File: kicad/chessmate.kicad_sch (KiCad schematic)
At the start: 41 parts, among them J1 7SegBtm, J2 Power Jack, J3 7SegTop, Q1 2N2222, Q2 2N2222, Q3 2N2222, Q4 2N2222, Q5 2N2222, SW1 F6, SW10 ENTER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

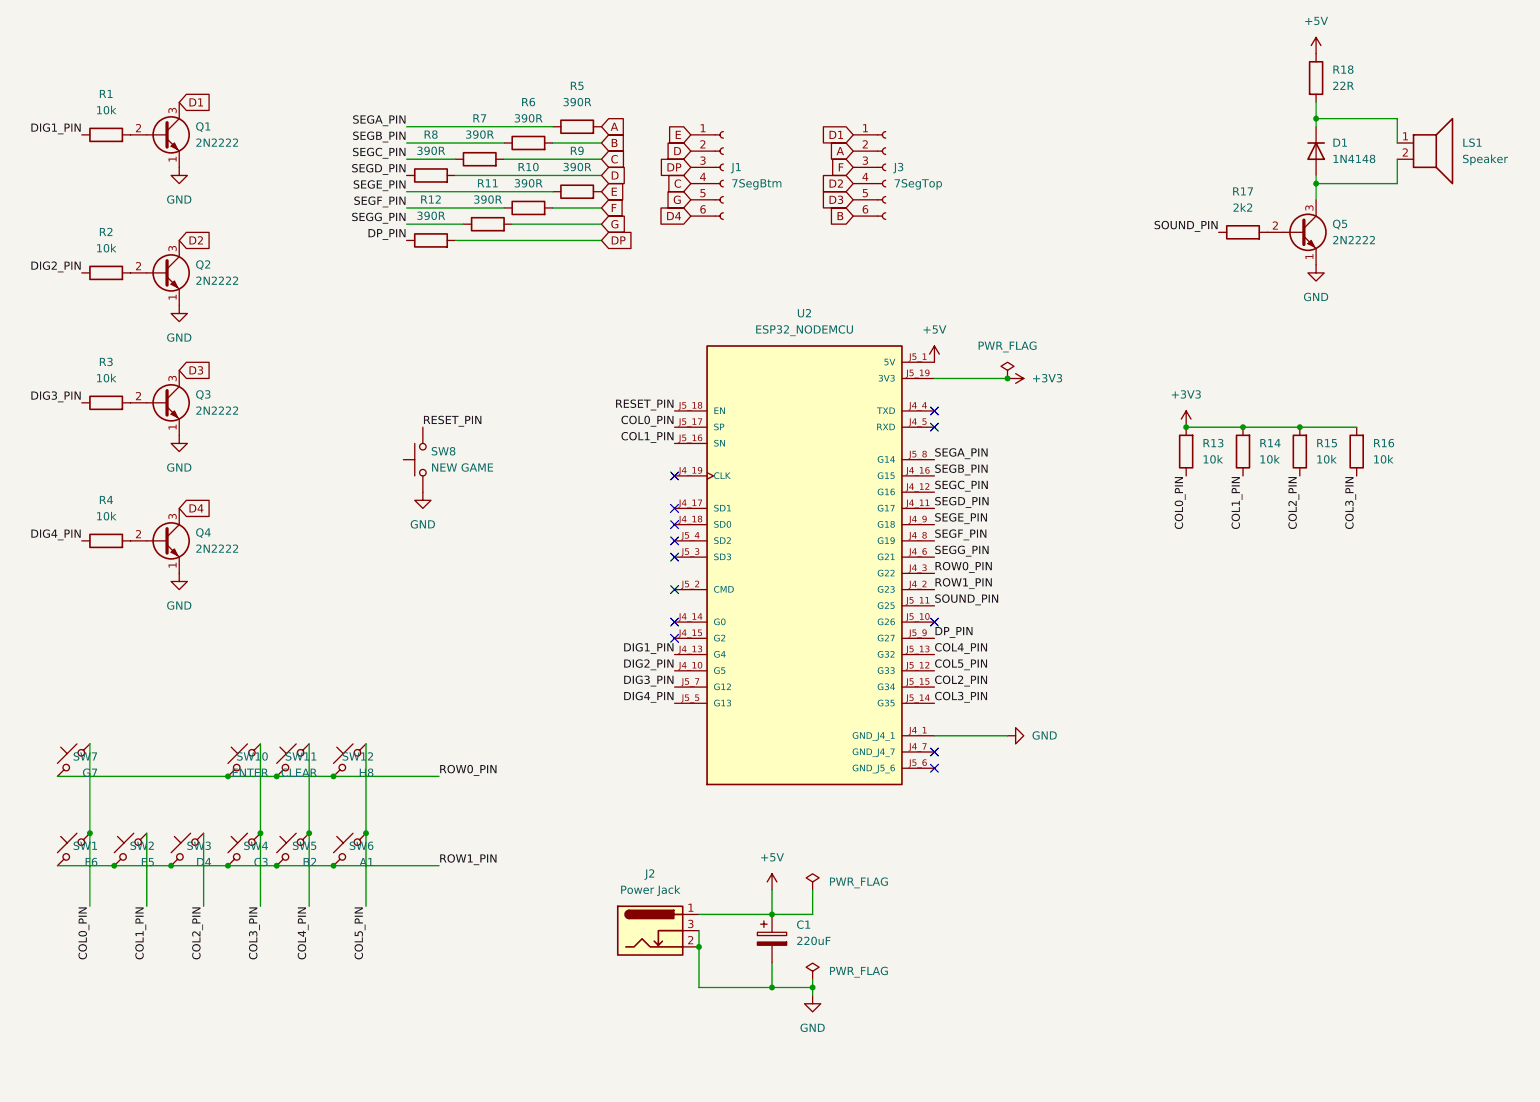
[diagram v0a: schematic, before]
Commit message: update nodemcu footprint
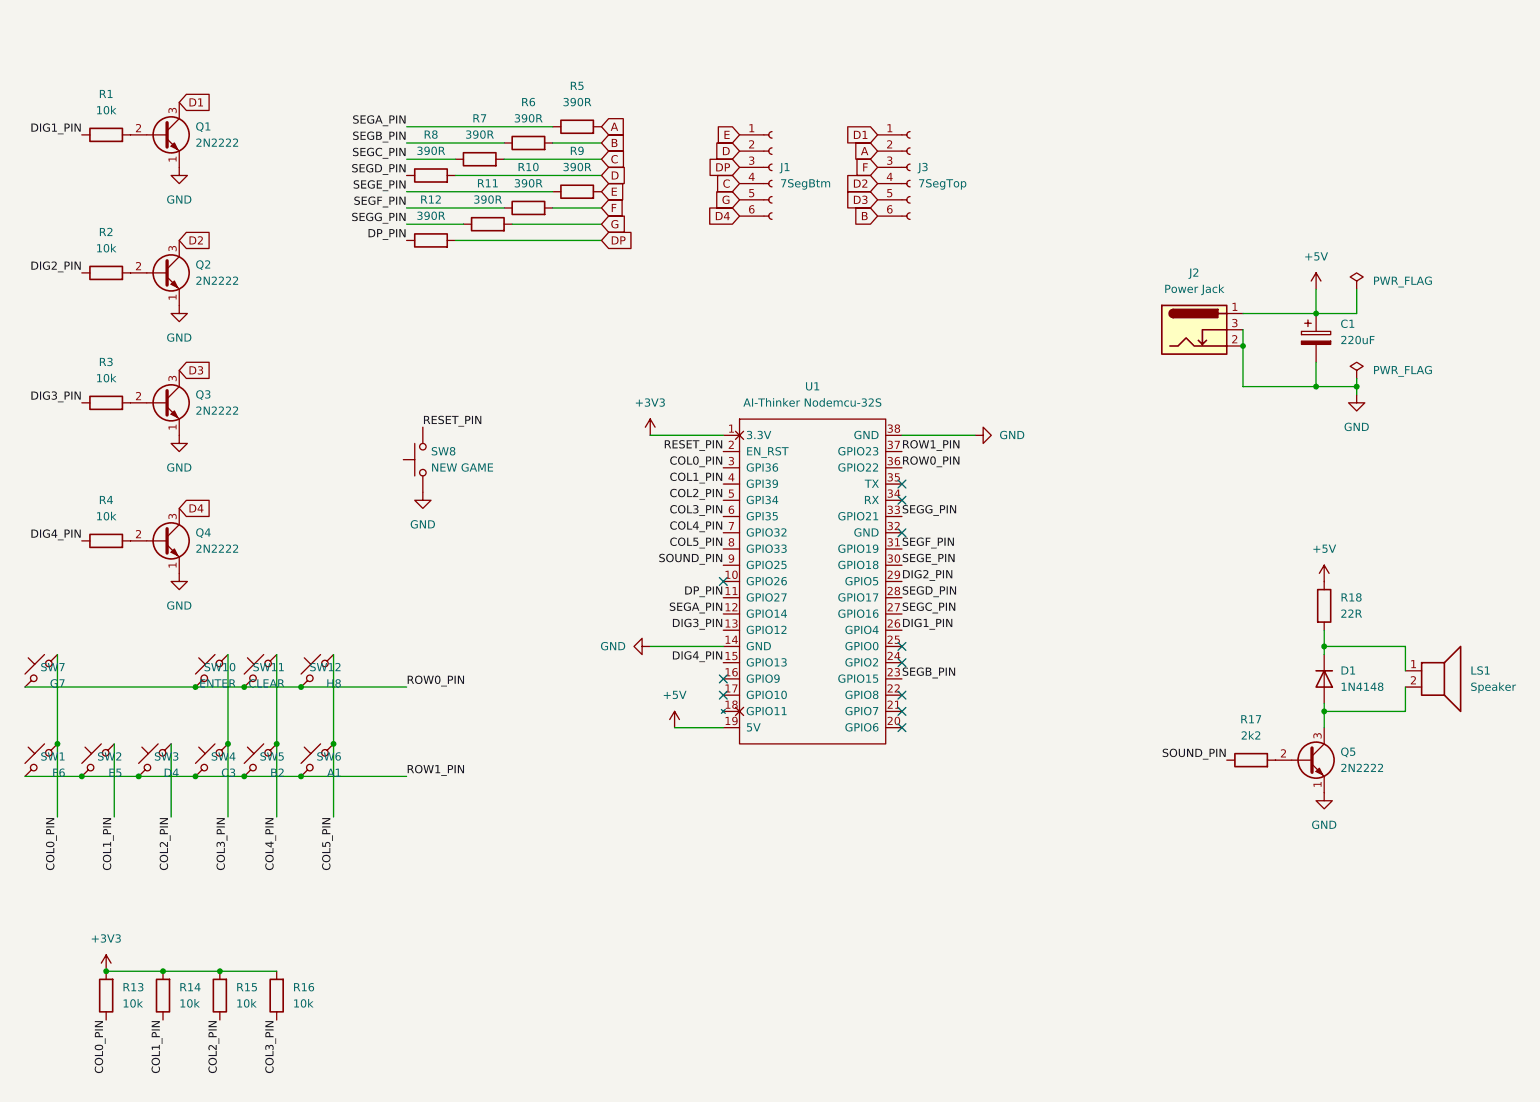
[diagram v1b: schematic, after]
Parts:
- removed U2: ESP32_NODEMCU, ESP32_NODEMCU:MODULE_ESP32_NODEMCU, symbol ESP32_NODEMCU:ESP32_NODEMCU
- added U1: AI-Thinker Nodemcu-32S, kicad-nodemcu32S-main:ai-thinker nodemcu-32s, symbol ai-thinker nodemcu-32s:AI-Thinker Nodemcu-32S
- LS1: footprint Buzzer_Beeper:Buzzer_12x9.5RM7.6 -> stevelib:Buzzer_12x9.5RM7.0
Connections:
- net +3V3: now also U1.1 (3.3V)
- net +5V: now also U1.19 (5V)
- net COL0_PIN: now also U1.3 (GPI36)
- net COL1_PIN: now also U1.4 (GPI39)
- net COL2_PIN: now also U1.5 (GPI34)
- net COL3_PIN: now also U1.6 (GPI35)
- net COL4_PIN: now also U1.7 (GPIO32)
- net COL5_PIN: now also U1.8 (GPIO33)
- net DIG1_PIN: now also U1.26 (GPIO4)
- net DIG2_PIN: now also U1.29 (GPIO5)
- net DIG3_PIN: now also U1.13 (GPIO12)
- net DIG4_PIN: now also U1.15 (GPIO13)
- net DP_PIN: now also U1.11 (GPIO27)
- net GND: now also U1.14 (GND), U1.38 (GND)
- net RESET_PIN: now also U1.2 (EN_RST)
- net ROW0_PIN: now also U1.36 (GPIO22)
- net ROW1_PIN: now also U1.37 (GPIO23)
- net SEGA_PIN: now also U1.12 (GPIO14)
- net SEGB_PIN: now also U1.23 (GPIO15)
- net SEGC_PIN: now also U1.27 (GPIO16)
- net SEGD_PIN: now also U1.28 (GPIO17)
- net SEGE_PIN: now also U1.30 (GPIO18)
- net SEGF_PIN: now also U1.31 (GPIO19)
- net SEGG_PIN: now also U1.33 (GPIO21)
- net SOUND_PIN: now also U1.9 (GPIO25)
- no-connect marks 13 -> 11
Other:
- moved on the sheet: C1, D1, J1, J2, J3, LS1, Q5, R13, R14, R15, R16, R17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

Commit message: move component values and switch names to F.Silkscreen layer
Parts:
- R13, R14, R15, R16: footprint Resistor_THT:R_Axial_DIN0204_L3.6mm_D1.6mm_P5.08mm_Horizontal -> Resistor_THT:R_Axial_DIN0207_L6.3mm_D2.5mm_P7.62mm_Horizontal
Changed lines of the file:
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@@
 			)
 		)
-		(property "Footprint" "Resistor_THT:R_Axial_DIN0204_L3.6mm_D1.6mm_P5.08mm_Horizontal"
+		(property "Footprint" "Resistor_THT:R_Axial_DIN0207_L6.3mm_D2.5mm_P7.62mm_Horizontal"
 			(at 48.768 175.26 90)
 			(effects
@@
 			)
 		)
-		(property "Footprint" "Resistor_THT:R_Axial_DIN0204_L3.6mm_D1.6mm_P5.08mm_Horizontal"
+		(property "Footprint" "Resistor_THT:R_Axial_DIN0207_L6.3mm_D2.5mm_P7.62mm_Horizontal"
 			(at 57.658 175.26 90)
 			(effects
@@
 			)
 		)
-		(property "Footprint" "Resistor_THT:R_Axial_DIN0204_L3.6mm_D1.6mm_P5.08mm_Horizontal"
+		(property "Footprint" "Resistor_THT:R_Axial_DIN0207_L6.3mm_D2.5mm_P7.62mm_Horizontal"
 			(at 66.548 175.26 90)
 			(effects
@@
 			)
 		)
-		(property "Footprint" "Resistor_THT:R_Axial_DIN0204_L3.6mm_D1.6mm_P5.08mm_Horizontal"
+		(property "Footprint" "Resistor_THT:R_Axial_DIN0207_L6.3mm_D2.5mm_P7.62mm_Horizontal"
 			(at 75.438 175.26 90)
 			(effects
